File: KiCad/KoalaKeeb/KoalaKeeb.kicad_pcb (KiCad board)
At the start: 2 copper layers, 236.6 x 86.3 mm, 62 parts, among them J1 JLC_Battery_Con_L, J2 JLC_Battery_Con_R, SW1 Switch_SW_Push, SW10 Switch_SW_Push, SW11 Switch_SW_Push, SW12 Switch_SW_Push, SW13 Switch_SW_Push, SW14 Switch_SW_Push, SW15 Switch_SW_Push, SW16 Switch_SW_Push, SW17 Switch_SW_Push, SW18 Switch_SW_Push, SW19 Switch_SW_Push, SW2 Switch_SW_Push, SW20 Switch_SW_Push, SW21 Switch_SW_Push, SW22 Switch_SW_Push, SW23 Switch_SW_Push, SW24 Switch_SW_Push, SW25 Switch_SW_Push, SW26 Switch_SW_Push, SW27 Switch_SW_Push, SW28 Switch_SW_Push, SW29 Switch_SW_Push, SW3 Switch_SW_Push, SW30 Switch_SW_Push, SW31 Switch_SW_Push, SW32 Switch_SW_Push, SW33 Switch_SW_Push, SW34 Switch_SW_Push, SW4 Switch_SW_Push, SW5 Switch_SW_Push, SW6 Switch_SW_Push, SW7 Switch_SW_Push, SW8 Switch_SW_Push, SW9 Switch_SW_Push, U1 Nice!Nano_L, U2 Nice!Nano_R

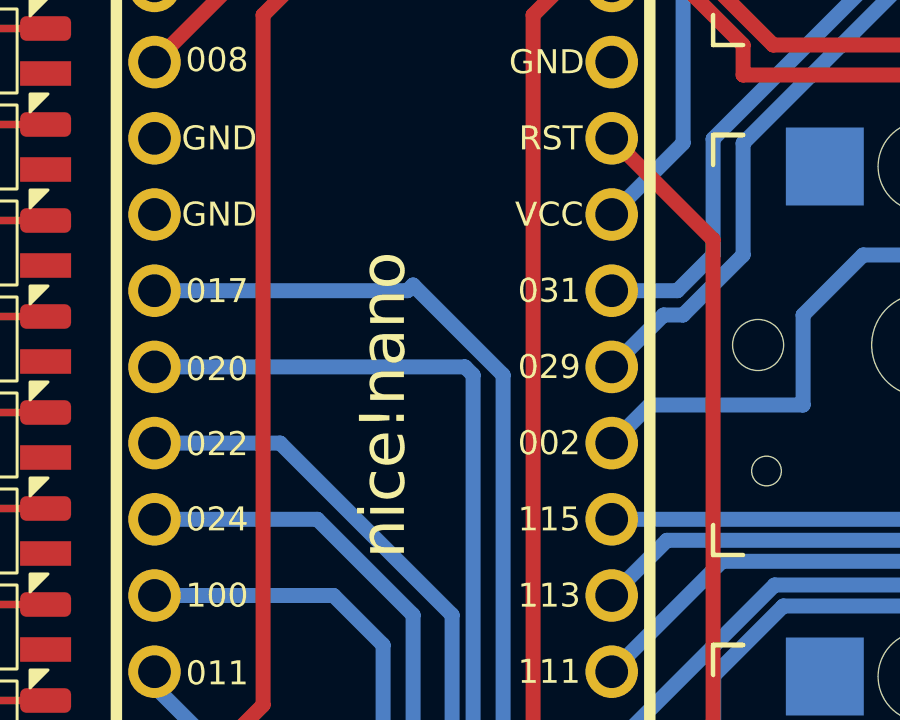
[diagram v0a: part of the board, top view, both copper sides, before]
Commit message: add text field for JLC serial number
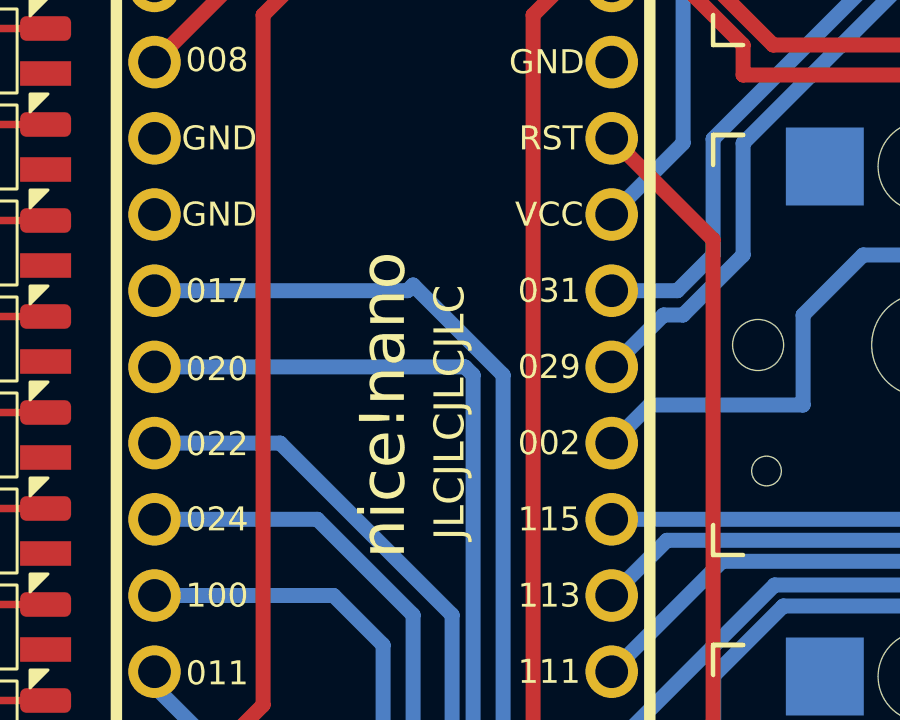
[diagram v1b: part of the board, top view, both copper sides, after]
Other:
- board text added: "JLCJLCJLCJLC"
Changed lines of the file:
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@@
       (plot_on_all_layers_selection 0x0000000_00000000)
       (disableapertmacros false)
-      (usegerberextensions false)
-      (usegerberattributes true)
-      (usegerberadvancedattributes true)
-      (creategerberjobfile true)
+      (usegerberextensions true)
+      (usegerberattributes false)
+      (usegerberadvancedattributes false)
+      (creategerberjobfile false)
       (dashed_line_dash_ratio 12.000000)
       (dashed_line_gap_ratio 3.000000)
@@
       (psa4output false)
       (plotreference true)
-      (plotvalue true)
+      (plotvalue false)
       (plotinvisibletext false)
       (sketchpadsonfab false)
-      (subtractmaskfromsilk false)
+      (subtractmaskfromsilk true)
       (outputformat 1)
       (mirror false)
@@
   (gr_arc (start 251.156265 38.411322) (mid 250.304796 38.058632) (end 249.952106 37.207163)
     (stroke (width 0.1) (type default)) (layer "Edge.Cuts"))
+  (gr_text "JLCJLCJLCJLC" (at 62.8 61.5 90) (layer "F.SilkS")
+    (effects (font (size 1 1) (thickness 0.15)) (justify left bottom))
+  )
   (segment (start 262.874296 77.625) (end 268.272853 83.023557) (width 0.5) (layer "F.Cu") (net 1))
   (segment (start 252.904 77.625) (end 262.874296 77.625) (width 0.5) (layer "F.Cu") (net 1))

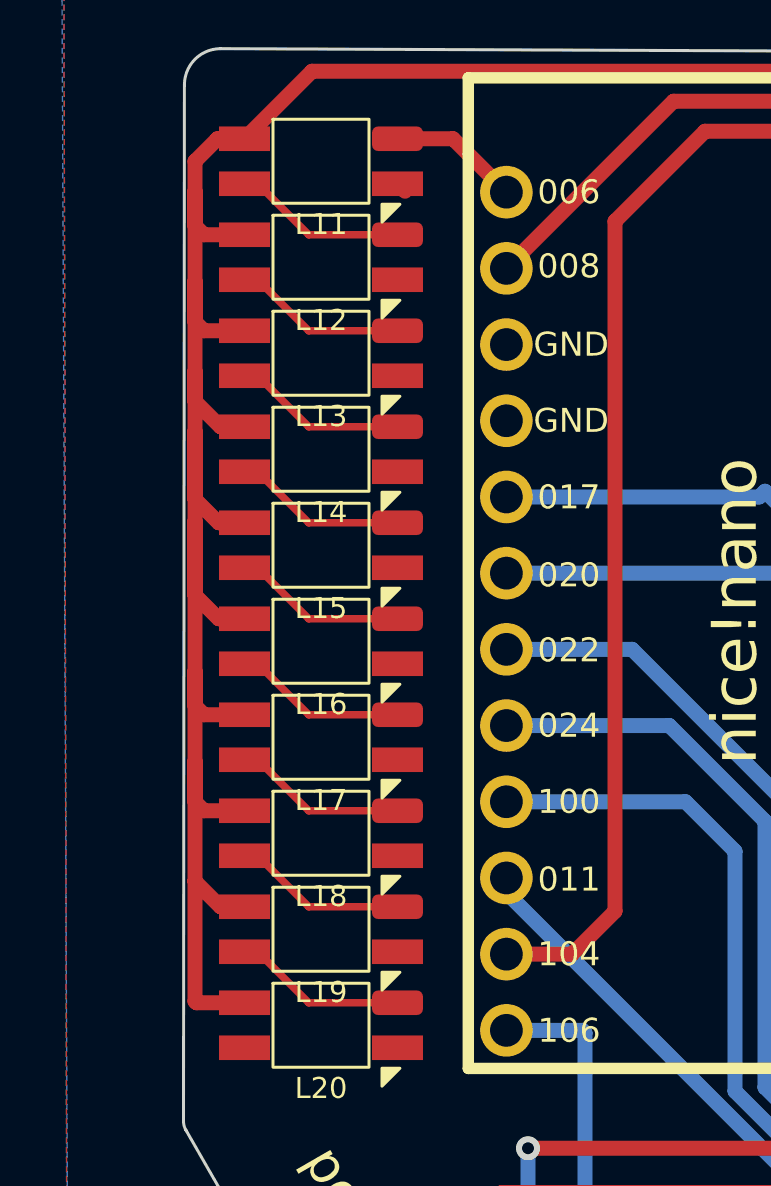
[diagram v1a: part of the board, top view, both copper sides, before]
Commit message: update routing for right half LEDs
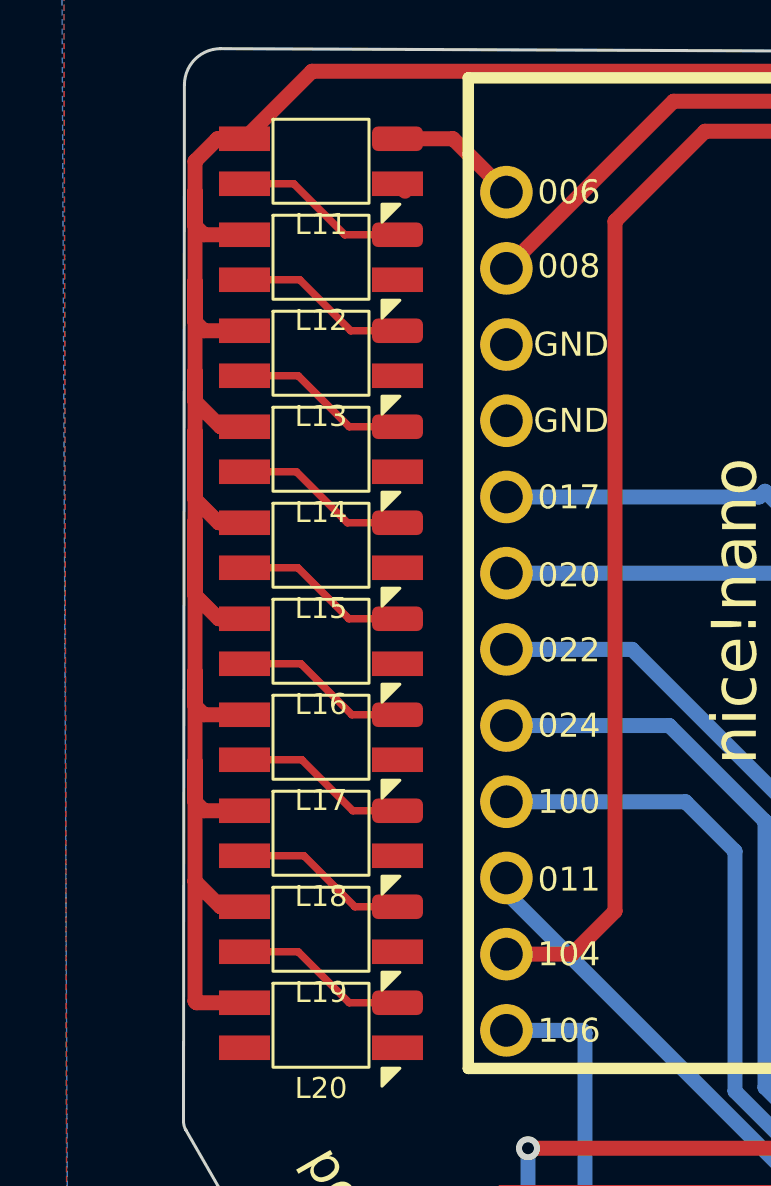
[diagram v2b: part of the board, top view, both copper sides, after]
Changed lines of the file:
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@@
   (segment (start 67.62 50.65) (end 70 48.27) (width 0.5) (layer "B.Cu") (net 17))
   (segment (start 70 48.27) (end 70 40) (width 0.5) (layer "B.Cu") (net 17))
-  (segment (start 44.09 42.75) (end 45.79 44.45) (width 0.25) (layer "F.Cu") (net 18))
-  (segment (start 43.65 42.75) (end 44.09 42.75) (width 0.25) (layer "F.Cu") (net 18))
-  (segment (start 45.79 44.45) (end 48.75 44.45) (width 0.25) (layer "F.Cu") (net 18))
+  (segment (start 46.99 44.45) (end 48.75 44.45) (width 0.25) (layer "F.Cu") (net 18))
+  (segment (start 43.65 42.75) (end 45.29 42.75) (width 0.25) (layer "F.Cu") (net 18))
+  (segment (start 45.29 42.75) (end 46.99 44.45) (width 0.25) (layer "F.Cu") (net 18))
   (segment (start 50.6 41.25) (end 48.75 41.25) (width 0.5) (layer "F.Cu") (net 19))
   (segment (start 52.38 43.03) (end 50.6 41.25) (width 0.5) (layer "F.Cu") (net 19))
-  (segment (start 44.09 45.95) (end 45.79 47.65) (width 0.25) (layer "F.Cu") (net 20))
-  (segment (start 43.65 45.95) (end 44.09 45.95) (width 0.25) (layer "F.Cu") (net 20))
-  (segment (start 45.79 47.65) (end 48.75 47.65) (width 0.25) (layer "F.Cu") (net 20))
-  (segment (start 43.65 49.15) (end 44.09 49.15) (width 0.25) (layer "F.Cu") (net 21))
-  (segment (start 45.79 50.85) (end 48.75 50.85) (width 0.25) (layer "F.Cu") (net 21))
-  (segment (start 44.09 49.15) (end 45.79 50.85) (width 0.25) (layer "F.Cu") (net 21))
-  (segment (start 45.79 54.05) (end 48.75 54.05) (width 0.25) (layer "F.Cu") (net 22))
-  (segment (start 43.65 52.35) (end 44.09 52.35) (width 0.25) (layer "F.Cu") (net 22))
-  (segment (start 44.09 52.35) (end 45.79 54.05) (width 0.25) (layer "F.Cu") (net 22))
-  (segment (start 43.65 55.55) (end 44.09 55.55) (width 0.25) (layer "F.Cu") (net 23))
-  (segment (start 45.79 57.25) (end 48.75 57.25) (width 0.25) (layer "F.Cu") (net 23))
-  (segment (start 44.09 55.55) (end 45.79 57.25) (width 0.25) (layer "F.Cu") (net 23))
-  (segment (start 43.65 58.75) (end 44.09 58.75) (width 0.25) (layer "F.Cu") (net 24))
-  (segment (start 44.09 58.75) (end 45.79 60.45) (width 0.25) (layer "F.Cu") (net 24))
-  (segment (start 45.79 60.45) (end 48.75 60.45) (width 0.25) (layer "F.Cu") (net 24))
-  (segment (start 44.09 61.95) (end 45.79 63.65) (width 0.25) (layer "F.Cu") (net 25))
-  (segment (start 45.79 63.65) (end 48.75 63.65) (width 0.25) (layer "F.Cu") (net 25))
-  (segment (start 43.65 61.95) (end 44.09 61.95) (width 0.25) (layer "F.Cu") (net 25))
-  (segment (start 43.65 65.15) (end 44.09 65.15) (width 0.25) (layer "F.Cu") (net 26))
-  (segment (start 45.79 66.85) (end 48.75 66.85) (width 0.25) (layer "F.Cu") (net 26))
-  (segment (start 44.09 65.15) (end 45.79 66.85) (width 0.25) (layer "F.Cu") (net 26))
-  (segment (start 43.65 68.35) (end 44.09 68.35) (width 0.25) (layer "F.Cu") (net 27))
-  (segment (start 45.79 70.05) (end 48.75 70.05) (width 0.25) (layer "F.Cu") (net 27))
-  (segment (start 44.09 68.35) (end 45.79 70.05) (width 0.25) (layer "F.Cu") (net 27))
+  (segment (start 43.65 45.95) (end 45.49 45.95) (width 0.25) (layer "F.Cu") (net 20))
+  (segment (start 47.19 47.65) (end 48.75 47.65) (width 0.25) (layer "F.Cu") (net 20))
+  (segment (start 45.49 45.95) (end 47.19 47.65) (width 0.25) (layer "F.Cu") (net 20))
+  (segment (start 47.14 50.85) (end 48.75 50.85) (width 0.25) (layer "F.Cu") (net 21))
+  (segment (start 43.65 49.15) (end 45.44 49.15) (width 0.25) (layer "F.Cu") (net 21))
+  (segment (start 45.44 49.15) (end 47.14 50.85) (width 0.25) (layer "F.Cu") (net 21))
+  (segment (start 45.38 52.35) (end 47.08 54.05) (width 0.25) (layer "F.Cu") (net 22))
+  (segment (start 47.08 54.05) (end 48.75 54.05) (width 0.25) (layer "F.Cu") (net 22))
+  (segment (start 43.65 52.35) (end 45.38 52.35) (width 0.25) (layer "F.Cu") (net 22))
+  (segment (start 45.43 55.55) (end 47.13 57.25) (width 0.25) (layer "F.Cu") (net 23))
+  (segment (start 47.13 57.25) (end 48.75 57.25) (width 0.25) (layer "F.Cu") (net 23))
+  (segment (start 43.65 55.55) (end 45.43 55.55) (width 0.25) (layer "F.Cu") (net 23))
+  (segment (start 47.23 60.45) (end 48.75 60.45) (width 0.25) (layer "F.Cu") (net 24))
+  (segment (start 45.53 58.75) (end 47.23 60.45) (width 0.25) (layer "F.Cu") (net 24))
+  (segment (start 43.65 58.75) (end 45.53 58.75) (width 0.25) (layer "F.Cu") (net 24))
+  (segment (start 45.56 61.95) (end 47.26 63.65) (width 0.25) (layer "F.Cu") (net 25))
+  (segment (start 47.26 63.65) (end 48.75 63.65) (width 0.25) (layer "F.Cu") (net 25))
+  (segment (start 43.65 61.95) (end 45.56 61.95) (width 0.25) (layer "F.Cu") (net 25))
+  (segment (start 43.65 65.15) (end 45.63 65.15) (width 0.25) (layer "F.Cu") (net 26))
+  (segment (start 47.33 66.85) (end 48.75 66.85) (width 0.25) (layer "F.Cu") (net 26))
+  (segment (start 45.63 65.15) (end 47.33 66.85) (width 0.25) (layer "F.Cu") (net 26))
+  (segment (start 45.44 68.35) (end 47.14 70.05) (width 0.25) (layer "F.Cu") (net 27))
+  (segment (start 47.14 70.05) (end 48.75 70.05) (width 0.25) (layer "F.Cu") (net 27))
+  (segment (start 43.65 68.35) (end 45.44 68.35) (width 0.25) (layer "F.Cu") (net 27))
   (segment (start 268.8 79.452628) (end 269.772853 80.425481) (width 0.5) (layer "F.Cu") (net 29))
   (segment (start 268.8 76.6) (end 268.8 79.452628) (width 0.5) (layer "F.Cu") (net 29))

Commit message: add logo and create gerber files
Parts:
- added G***: LOGO, KoalaKeeb:Koalalogo, F.Cu at (114.0, 86.0)
- added G***: LOGO, KoalaKeeb:Koalalogo_mirrored, F.Cu at (206.0, 86.0)
